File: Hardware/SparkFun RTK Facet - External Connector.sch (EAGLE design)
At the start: 22 parts, among them J1 FPC_12_0.5MM2, J4 Qwiic, J5 u-blox USB, J6 FPC_12_0.5MM2

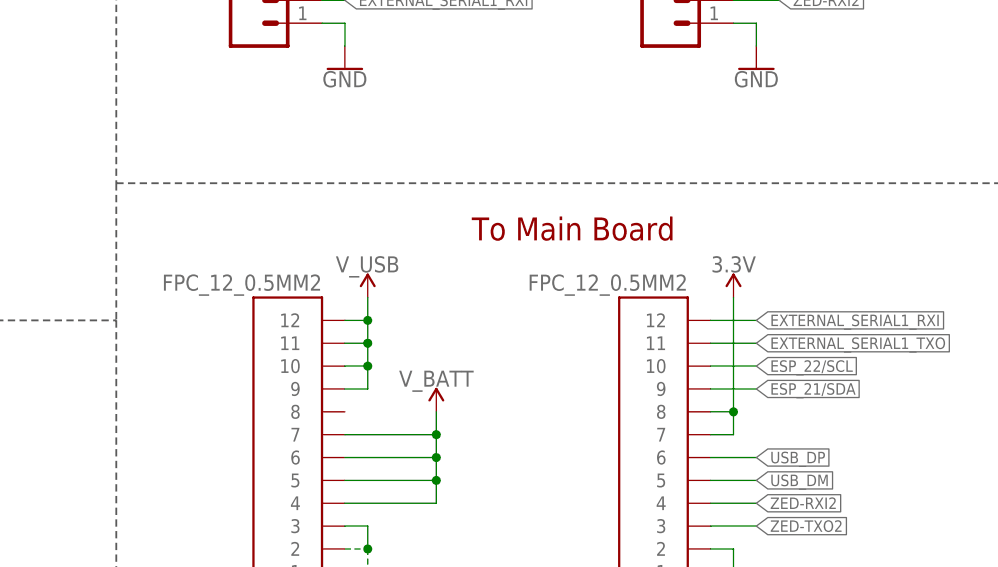
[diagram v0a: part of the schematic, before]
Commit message: Update PROD ID on 12 pin connector. Add gerbers for v10.
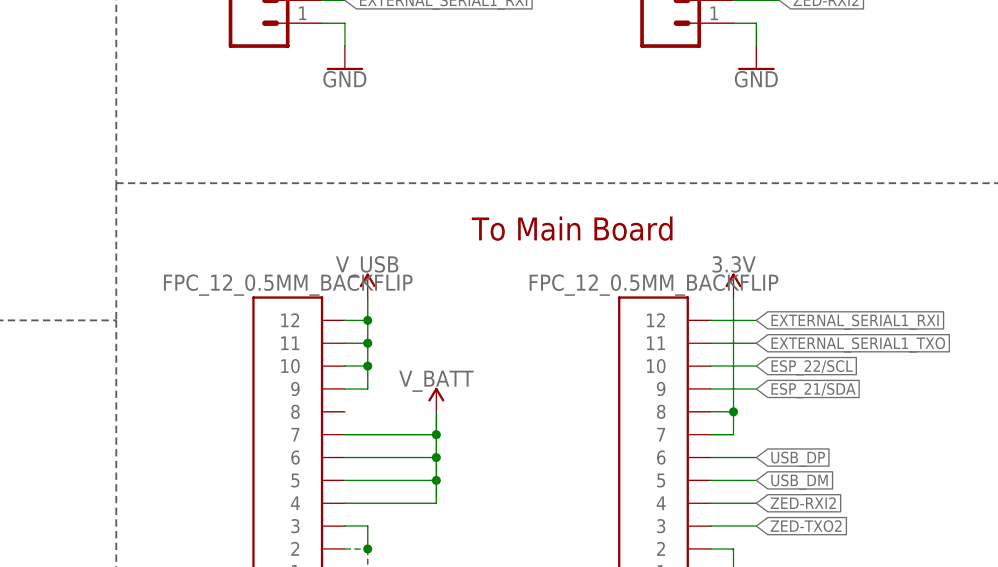
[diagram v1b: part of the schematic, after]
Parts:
- J1, J6: value FPC_12_0.5MM2 -> FPC_12_0.5MM_BACKFLIP; device RTK Facet:FPC_12_0.5MM2 -> RTK Facet:FPC_12_0.5MM_BACKFLIP
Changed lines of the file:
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@@
 <part name="SUPPLY3" library="SparkFun-PowerSymbols" deviceset="V_USB" device=""/>
 <part name="F3" library="SparkFun-Fuses" deviceset="PPTC" device="_6V2A" value="6V/2A"/>
-<part name="J1" library="RTK Facet" deviceset="FPC_12_0.5MM" device="2" value="FPC_12_0.5MM2"/>
-<part name="J6" library="RTK Facet" deviceset="FPC_12_0.5MM" device="2" value="FPC_12_0.5MM2"/>
+<part name="J1" library="RTK Facet" deviceset="FPC_12_0.5MM" device="_BACKFLIP" value="FPC_12_0.5MM_BACKFLIP"/>
+<part name="J6" library="RTK Facet" deviceset="FPC_12_0.5MM" device="_BACKFLIP" value="FPC_12_0.5MM_BACKFLIP"/>
 </parts>
 <sheets>
